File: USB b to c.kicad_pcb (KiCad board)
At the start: 2 copper layers, 12 x 16.7 mm, 4 parts, among them J1 USB_C_Receptacle_USB2.0, J2 USB_B

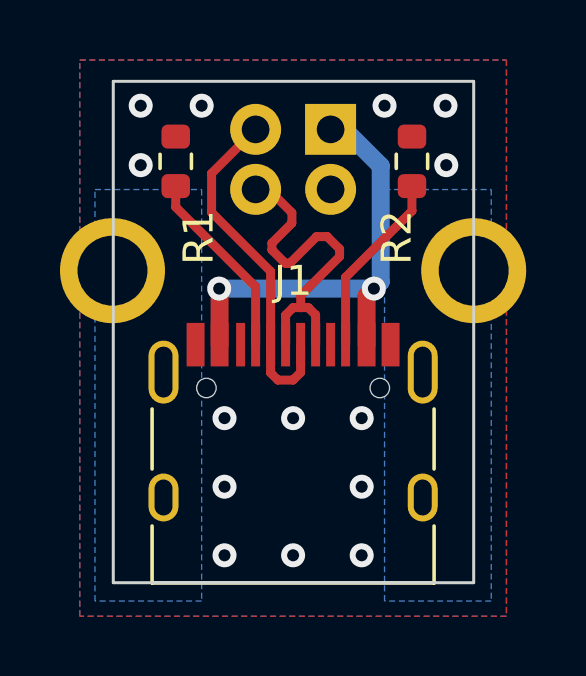
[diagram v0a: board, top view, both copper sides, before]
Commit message: Shifted USB D- for even trace spacing
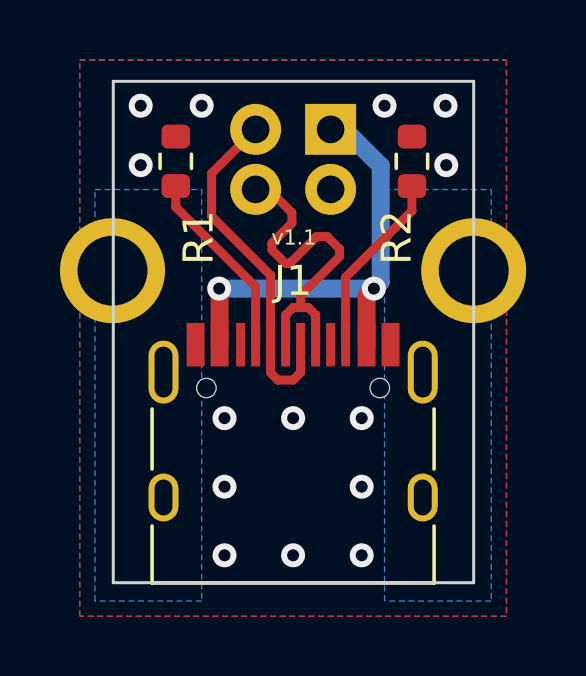
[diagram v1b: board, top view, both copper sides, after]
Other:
- board text added: "NICK LEKAS 2022/01/30"
- board text added: "v1.1"
- board text removed: "NICK LEKAS v1.1 2022/01/30"
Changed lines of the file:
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@@
     )
     (pad_to_mask_clearance 0.0508)
-    (solder_mask_min_width 0.101)
     (grid_origin 99.3394 101.2952)
     (pcbplotparams
@@
       (psa4output false)
       (plotreference true)
-      (plotvalue false)
+      (plotvalue true)
       (plotinvisibletext false)
       (sketchpadsonfab false)
@@
       (drillshape 0)
       (scaleselection 1)
-      (outputdirectory "C:/Users/Nick/Documents/NanoVNA type-c/fab/")
+      (outputdirectory "USB b to c fab/")
     )
   )
@@
   )
   (gr_rect (start 95.6056 98.5012) (end 107.6198 115.2144) (layer "Edge.Cuts") (width 0.1) (fill none))
-  (gr_text "NICK LEKAS\n\nv1.1\n2022/01/30" (at 101.6254 111.9632) (layer "B.SilkS")
+  (gr_text "NICK LEKAS\n\n\n2022/01/30" (at 101.6254 111.9632) (layer "B.SilkS")
     (effects (font (size 0.5 0.5) (thickness 0.125)) (justify mirror))
+  )
+  (gr_text "v1.1" (at 101.6254 103.7082) (layer "F.SilkS")
+    (effects (font (size 0.5 0.5) (thickness 0.125)))
   )
   (segment (start 101.33965 104.56545) (end 100.89515 104.12095) (width 0.3) (layer "F.Cu") (net 2))
@@
   (segment (start 103.35 107.278) (end 103.35 105.0316) (width 0.3) (layer "F.Cu") (net 3))
   (segment (start 103.35 105.0316) (end 105.5624 102.8192) (width 0.3) (layer "F.Cu") (net 3))
-  (segment (start 98.8822 102.87) (end 100.85 104.8378) (width 0.3) (layer "F.Cu") (net 5))
   (segment (start 100.35 100.1025) (end 98.8822 101.5703) (width 0.3) (layer "F.Cu") (net 5))
+  (segment (start 100.85 104.9648) (end 100.85 107.278) (width 0.3) (layer "F.Cu") (net 5))
   (segment (start 101.85 107.278) (end 101.85 108.208) (width 0.3) (layer "F.Cu") (net 5))
+  (segment (start 98.8822 101.5703) (end 98.8822 102.997) (width 0.3) (layer "F.Cu") (net 5))
   (segment (start 101.85 108.208) (end 101.6 108.458) (width 0.3) (layer "F.Cu") (net 5))
-  (segment (start 100.85 104.8378) (end 100.85 107.278) (width 0.3) (layer "F.Cu") (net 5))
   (segment (start 100.85 108.216) (end 101.092 108.458) (width 0.3) (layer "F.Cu") (net 5))
+  (segment (start 98.8822 102.997) (end 100.85 104.9648) (width 0.3) (layer "F.Cu") (net 5))
   (segment (start 100.85 107.278) (end 100.85 108.216) (width 0.3) (layer "F.Cu") (net 5))
-  (segment (start 98.8822 101.5703) (end 98.8822 102.87) (width 0.3) (layer "F.Cu") (net 5))
   (segment (start 101.092 108.458) (end 101.6 108.458) (width 0.3) (layer "F.Cu") (net 5))
   (segment (start 100.35 105.3538) (end 97.6884 102.6922) (width 0.3) (layer "F.Cu") (net 6))
